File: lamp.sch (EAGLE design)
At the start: 57 parts

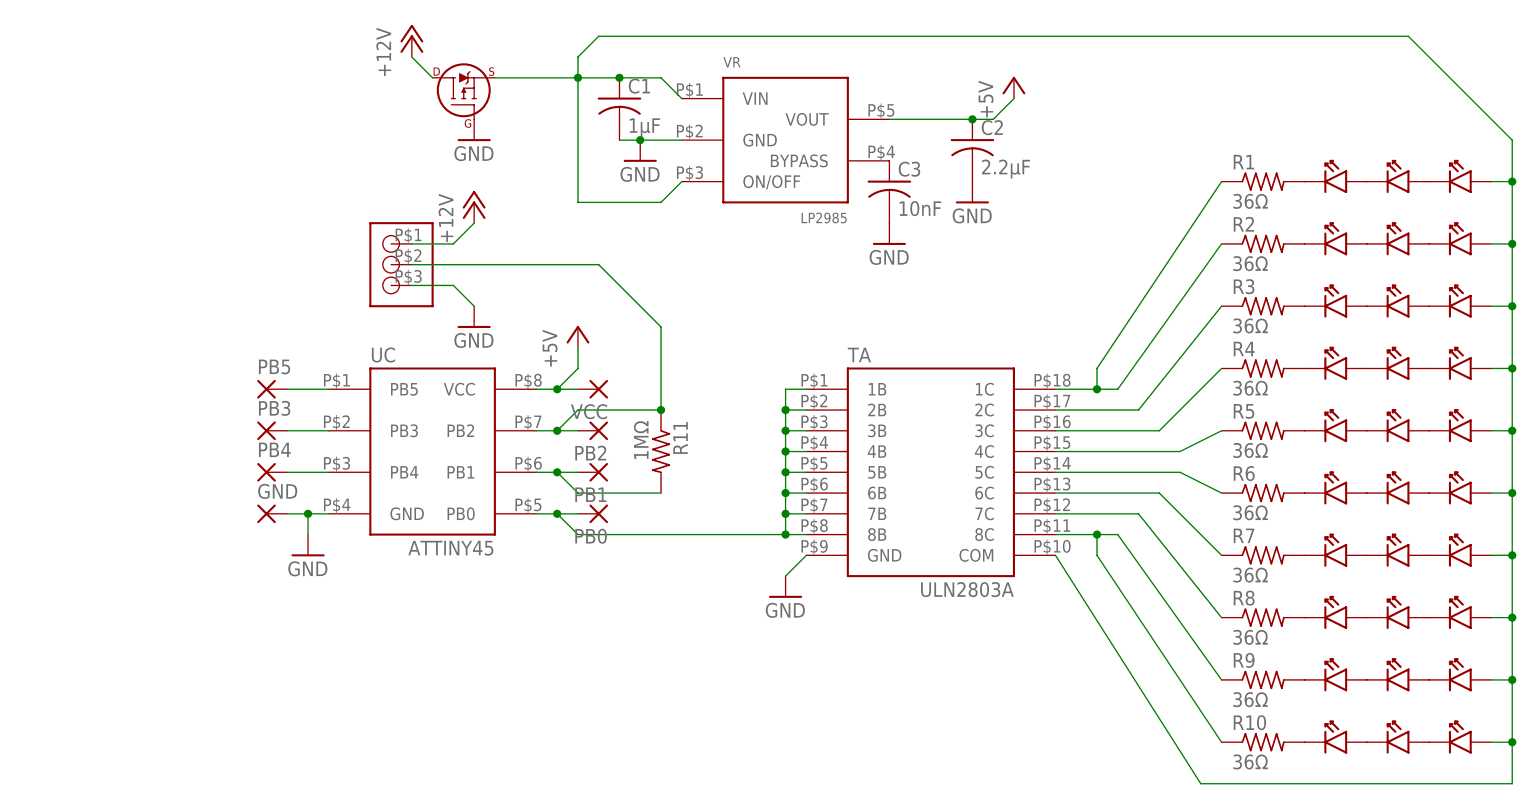
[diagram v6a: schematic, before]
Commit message: Swapped pins around on attiny45 for a better layout, adjusted layout accordingly. Much cleaner now.
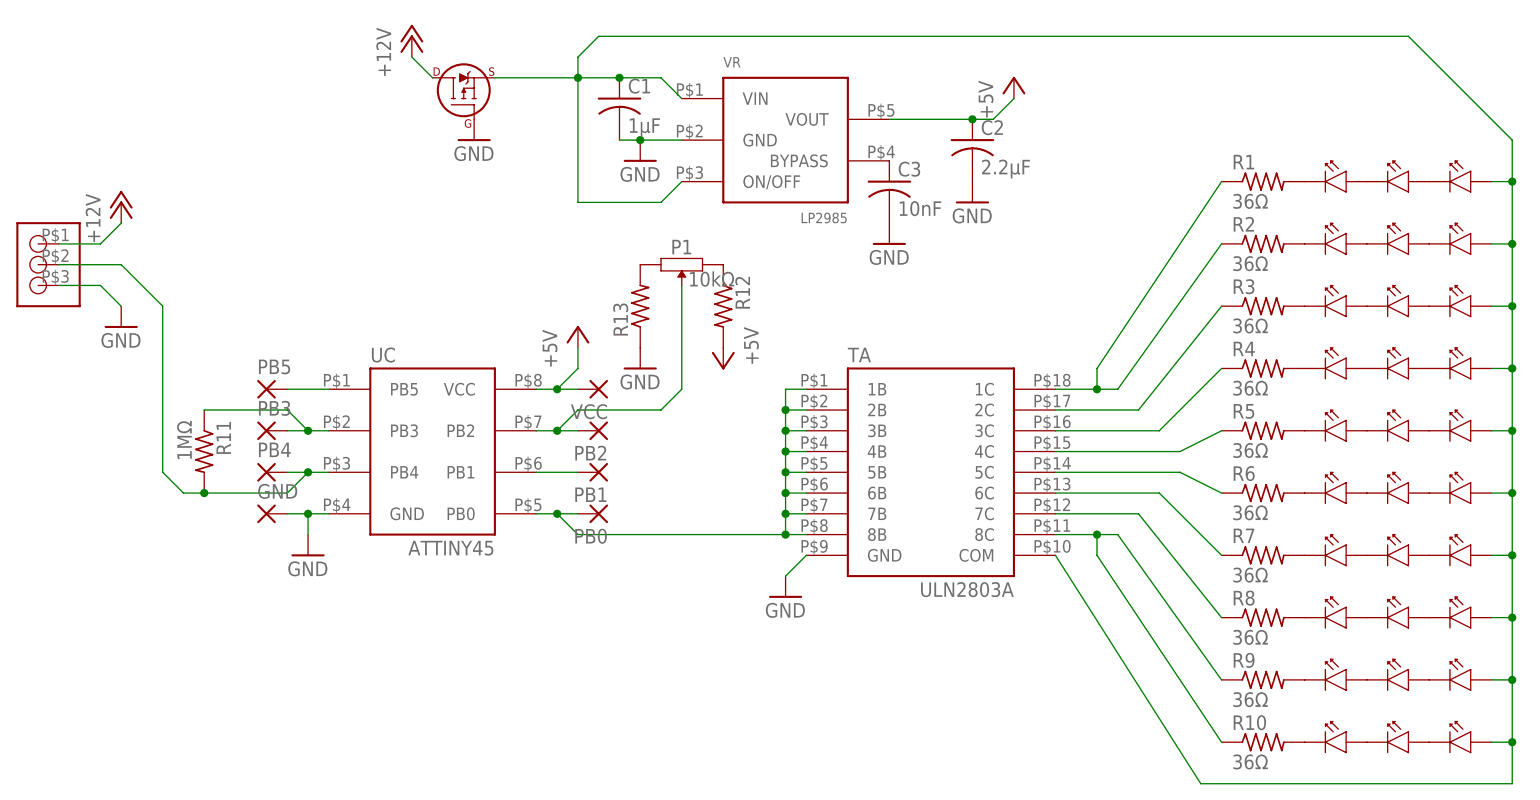
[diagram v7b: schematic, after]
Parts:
- added P1: 10kΩ, lamp:PVG3G
- added R12, R13: (no value), Barebones-Arduino:RESISTOR-SMD
- renumbered U$19 to F1
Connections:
- net +12V renamed N$49
- removed net N$14: PB1.P, R11.2, UC.PB1
- removed net N$39: PB3.P, UC.PB3
- new net N$50: P1.P$2, PB2.P, UC.PB2
- new net N$51: PB3.P, R11.1, UC.PB3
- new net N$52: PB1.P, UC.PB1
- net +5V: now also C2.1, R12.2, VR.VOUT
- net GND: now also R13.1
- net N$15: now also PB4.P, R11.2, U$32.P$2, UC.PB4; no longer C2.1, VR.VOUT
- net N$17: now also P1.P$3, R12.1; no longer PB2.P, R11.1, U$32.P$2, UC.PB2
- net N$44: now also P1.P$1, R13.2; no longer PB4.P, UC.PB4
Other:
- moved on the sheet: R11
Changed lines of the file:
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@@
 <part name="GND4" library=" Barebones-Arduino" deviceset="GND" device=""/>
 <part name="R11" library=" Barebones-Arduino" deviceset="RESISTOR" device="-SMD" value="1MΩ"/>
-<part name="U$19" library="lamp" deviceset="SI2319DS" device=""/>
+<part name="F1" library="lamp" deviceset="SI2319DS" device=""/>
 <part name="GND6" library=" Barebones-Arduino" deviceset="GND" device=""/>
 <part name="U$32" library="lamp" deviceset="HEADER-3X1" device=""/>
 <part name="P+5" library=" Barebones-Arduino" deviceset="+12V" device=""/>
 <part name="GND7" library=" Barebones-Arduino" deviceset="GND" device=""/>
+<part name="P1" library="lamp" deviceset="PVG3G" device="" value="10kΩ"/>
+<part name="R12" library=" Barebones-Arduino" deviceset="RESISTOR" device="-SMD"/>
+<part name="R13" library=" Barebones-Arduino" deviceset="RESISTOR" device="-SMD"/>
+<part name="P+1" library=" Barebones-Arduino" deviceset="+5V" device=""/>
+<part name="GND8" library=" Barebones-Arduino" deviceset="GND" device=""/>
 </parts>
 <sheets>
@@
 <instance part="C3" gate="G$1" x="58.42" y="76.2"/>
 <instance part="GND4" gate="1" x="58.42" y="68.58"/>
-<instance part="R11" gate="G$1" x="30.48" y="43.18" rot="R270"/>
-<instance part="U$19" gate="G$1" x="5.08" y="88.9"/>
+<instance part="R11" gate="G$1" x="-25.4" y="43.18" rot="R270"/>
+<instance part="F1" gate="G$1" x="5.08" y="88.9"/>
 <instance part="GND6" gate="1" x="7.62" y="81.28"/>
-<instance part="U$32" gate="G$1" x="0" y="68.58"/>
-<instance part="P+5" gate="1" x="7.62" y="73.66"/>
-<instance part="GND7" gate="1" x="7.62" y="58.42"/>
+<instance part="U$32" gate="G$1" x="-43.18" y="68.58"/>
+<instance part="P+5" gate="1" x="-35.56" y="73.66"/>
+<instance part="GND7" gate="1" x="-35.56" y="58.42"/>
+<instance part="P1" gate="G$1" x="33.02" y="66.04" rot="R90"/>
+<instance part="R12" gate="G$1" x="38.1" y="60.96" rot="R270"/>
+<instance part="R13" gate="G$1" x="27.94" y="60.96" rot="R90"/>
+<instance part="P+1" gate="1" x="38.1" y="53.34" rot="R180"/>
+<instance part="GND8" gate="1" x="27.94" y="53.34"/>
 </instances>
 <busses>
@@
 </segment>
 </net>
-<net name="+12V" class="0">
+<net name="N$49" class="0">
 <segment>
 <pinref part="P+3" gate="1" pin="+12V"/>
-<pinref part="U$19" gate="G$1" pin="DRAIN"/>
+<pinref part="F1" gate="G$1" pin="DRAIN"/>
 <wire x1="0" y1="91.44" x2="2.54" y2="88.9" width="0.1524" layer="91"/>
 </segment>
 <segment>
 <pinref part="U$32" gate="G$1" pin="P$1"/>
-<wire x1="0" y1="68.58" x2="5.08" y2="68.58" width="0.1524" layer="91"/>
-<wire x1="5.08" y1="68.58" x2="7.62" y2="71.12" width="0.1524" layer="91"/>
+<wire x1="-43.18" y1="68.58" x2="-38.1" y2="68.58" width="0.1524" layer="91"/>
+<wire x1="-38.1" y1="68.58" x2="-35.56" y2="71.12" width="0.1524" layer="91"/>
 <pinref part="P+5" gate="1" pin="+12V"/>
 </segment>
@@
 </segment>
 <segment>
-<pinref part="U$19" gate="G$1" pin="GATE"/>
+<pinref part="F1" gate="G$1" pin="GATE"/>
 <pinref part="GND6" gate="1" pin="GND"/>
 </segment>
 <segment>
 <pinref part="U$32" gate="G$1" pin="P$3"/>
-<wire x1="0" y1="63.5" x2="5.08" y2="63.5" width="0.1524" layer="91"/>
-<wire x1="7.62" y1="60.96" x2="5.08" y2="63.5" width="0.1524" layer="91"/>
+<wire x1="-43.18" y1="63.5" x2="-38.1" y2="63.5" width="0.1524" layer="91"/>
+<wire x1="-35.56" y1="60.96" x2="-38.1" y2="63.5" width="0.1524" layer="91"/>
 <pinref part="GND7" gate="1" pin="GND"/>
 </segment>
-</net>
-<net name="N$15" class="0">
-<segment>
-<pinref part="P+4" gate="1" pin="+5V"/>
-<wire x1="73.66" y1="86.36" x2="71.12" y2="83.82" width="0.1524" layer="91"/>
-<pinref part="VR" gate="G$1" pin="VOUT"/>
-<pinref part="C2" gate="G$1" pin="1"/>
-<wire x1="58.42" y1="83.82" x2="68.58" y2="83.82" width="0.1524" layer="91"/>
-<junction x="68.58" y="83.82"/>
-<wire x1="71.12" y1="83.82" x2="68.58" y2="83.82" width="0.1524" layer="91"/>
-</segment>
-</net>
-<net name="N$14" class="0">
-<segment>
-<pinref part="UC" gate="G$1" pin="PB1"/>
-<pinref part="PB1" gate="1" pin="P"/>
-<wire x1="15.24" y1="40.64" x2="17.78" y2="40.64" width="0.1524" layer="91"/>
-<pinref part="R11" gate="G$1" pin="2"/>
-<wire x1="17.78" y1="40.64" x2="20.32" y2="40.64" width="0.1524" layer="91"/>
-<wire x1="17.78" y1="40.64" x2="20.32" y2="38.1" width="0.1524" layer="91"/>
-<wire x1="20.32" y1="38.1" x2="30.48" y2="38.1" width="0.1524" layer="91"/>
-<junction x="17.78" y="40.64"/>
-</segment>
-</net>
-<net name="N$17" class="0">
-<segment>
-<pinref part="UC" gate="G$1" pin="PB2"/>
-<pinref part="PB2" gate="1" pin="P"/>
-<wire x1="15.24" y1="45.72" x2="17.78" y2="45.72" width="0.1524" layer="91"/>
-<pinref part="R11" gate="G$1" pin="1"/>
-<wire x1="17.78" y1="45.72" x2="20.32" y2="45.72" width="0.1524" layer="91"/>
-<wire x1="17.78" y1="45.72" x2="20.32" y2="48.26" width="0.1524" layer="91"/>
-<wire x1="20.32" y1="48.26" x2="30.48" y2="48.26" width="0.1524" layer="91"/>
-<junction x="17.78" y="45.72"/>
-<junction x="30.48" y="48.26"/>
-<pinref part="U$32" gate="G$1" pin="P$2"/>
-<wire x1="0" y1="66.04" x2="22.86" y2="66.04" width="0.1524" layer="91"/>
-<wire x1="22.86" y1="66.04" x2="30.48" y2="58.42" width="0.1524" layer="91"/>
-<wire x1="30.48" y1="58.42" x2="30.48" y2="48.26" width="0.1524" layer="91"/>
+<segment>
+<pinref part="R13" gate="G$1" pin="1"/>
+<pinref part="GND8" gate="1" pin="GND"/>
 </segment>
 </net>
@@
 <pinref part="PB5" gate="1" pin="P"/>
 <wire x1="-10.16" y1="50.8" x2="-15.24" y2="50.8" width="0.1524" layer="91"/>
-</segment>
-</net>
-<net name="N$39" class="0">
-<segment>
-<pinref part="UC" gate="G$1" pin="PB3"/>
-<pinref part="PB3" gate="1" pin="P"/>
-<wire x1="-10.16" y1="45.72" x2="-15.24" y2="45.72" width="0.1524" layer="91"/>
-</segment>
-</net>
-<net name="N$44" class="0">
-<segment>
-<pinref part="UC" gate="G$1" pin="PB4"/>
-<pinref part="PB4" gate="1" pin="P"/>
-<wire x1="-10.16" y1="40.64" x2="-15.24" y2="40.64" width="0.1524" layer="91"/>
 </segment>
 </net>
@@
 <junction x="17.78" y="50.8"/>
 </segment>
+<segment>
+<pinref part="P+4" gate="1" pin="+5V"/>
+<wire x1="73.66" y1="86.36" x2="71.12" y2="83.82" width="0.1524" layer="91"/>
+<pinref part="VR" gate="G$1" pin="VOUT"/>
+<pinref part="C2" gate="G$1" pin="1"/>
+<wire x1="58.42" y1="83.82" x2="68.58" y2="83.82" width="0.1524" layer="91"/>
+<junction x="68.58" y="83.82"/>
+<wire x1="71.12" y1="83.82" x2="68.58" y2="83.82" width="0.1524" layer="91"/>
+</segment>
+<segment>
+<pinref part="R12" gate="G$1" pin="2"/>
+<pinref part="P+1" gate="1" pin="+5V"/>
+</segment>
 </net>
 <net name="N$45" class="0">
@@
 <pinref part="VR" gate="G$1" pin="VIN"/>
 <wire x1="30.48" y1="88.9" x2="33.02" y2="86.36" width="0.1524" layer="91"/>
-<pinref part="U$19" gate="G$1" pin="SOURCE"/>
+<pinref part="F1" gate="G$1" pin="SOURCE"/>
 <wire x1="10.16" y1="88.9" x2="20.32" y2="88.9" width="0.1524" layer="91"/>
 <junction x="20.32" y="88.9"/>
@@
 </segment>
 </net>
+<net name="N$15" class="0">
+<segment>
+<pinref part="PB4" gate="1" pin="P"/>
+<pinref part="UC" gate="G$1" pin="PB4"/>
+<wire x1="-10.16" y1="40.64" x2="-12.7" y2="40.64" width="0.1524" layer="91"/>
+<pinref part="R11" gate="G$1" pin="2"/>
+<wire x1="-12.7" y1="40.64" x2="-15.24" y2="40.64" width="0.1524" layer="91"/>
+<wire x1="-12.7" y1="40.64" x2="-15.24" y2="38.1" width="0.1524" layer="91"/>
+<wire x1="-15.24" y1="38.1" x2="-25.4" y2="38.1" width="0.1524" layer="91"/>
+<junction x="-12.7" y="40.64"/>
+<wire x1="-25.4" y1="38.1" x2="-27.94" y2="38.1" width="0.1524" layer="91"/>
+<junction x="-25.4" y="38.1"/>
+<wire x1="-27.94" y1="38.1" x2="-30.48" y2="40.64" width="0.1524" layer="91"/>
+<wire x1="-30.48" y1="40.64" x2="-30.48" y2="60.96" width="0.1524" layer="91"/>
+<pinref part="U$32" gate="G$1" pin="P$2"/>
+<wire x1="-30.48" y1="60.96" x2="-35.56" y2="66.04" width="0.1524" layer="91"/>
+<wire x1="-35.56" y1="66.04" x2="-43.18" y2="66.04" width="0.1524" layer="91"/>
+</segment>
+</net>
+<net name="N$17" class="0">
+<segment>
+<pinref part="P1" gate="G$1" pin="P$3"/>
+<pinref part="R12" gate="G$1" pin="1"/>
+</segment>
+</net>
+<net name="N$44" class="0">
+<segment>
+<pinref part="P1" gate="G$1" pin="P$1"/>
+<pinref part="R13" gate="G$1" pin="2"/>
+</segment>
+</net>
+<net name="N$50" class="0">
+<segment>
+<pinref part="PB2" gate="1" pin="P"/>
+<pinref part="UC" gate="G$1" pin="PB2"/>
+<wire x1="15.24" y1="45.72" x2="17.78" y2="45.72" width="0.1524" layer="91"/>
+<wire x1="17.78" y1="45.72" x2="20.32" y2="45.72" width="0.1524" layer="91"/>
+<wire x1="17.78" y1="45.72" x2="20.32" y2="48.26" width="0.1524" layer="91"/>
+<wire x1="20.32" y1="48.26" x2="30.48" y2="48.26" width="0.1524" layer="91"/>
+<junction x="17.78" y="45.72"/>
+<pinref part="P1" gate="G$1" pin="P$2"/>
+<wire x1="30.48" y1="48.26" x2="33.02" y2="50.8" width="0.1524" layer="91"/>
+<wire x1="33.02" y1="50.8" x2="33.02" y2="63.5" width="0.1524" layer="91"/>
+</segment>
+</net>
+<net name="N$52" class="0">
+<segment>
+<pinref part="PB1" gate="1" pin="P"/>
+<pinref part="UC" gate="G$1" pin="PB1"/>
+<wire x1="15.24" y1="40.64" x2="20.32" y2="40.64" width="0.1524" layer="91"/>
+</segment>
+</net>
+<net name="N$51" class="0">
+<segment>
+<pinref part="R11" gate="G$1" pin="1"/>
+<pinref part="PB3" gate="1" pin="P"/>
+<pinref part="UC" gate="G$1" pin="PB3"/>
+<wire x1="-10.16" y1="45.72" x2="-12.7" y2="45.72" width="0.1524" layer="91"/>
+<wire x1="-12.7" y1="45.72" x2="-15.24" y2="45.72" width="0.1524" layer="91"/>
+<junction x="-12.7" y="45.72"/>
+<wire x1="-12.7" y1="45.72" x2="-15.24" y2="48.26" width="0.1524" layer="91"/>
+<wire x1="-15.24" y1="48.26" x2="-25.4" y2="48.26" width="0.1524" layer="91"/>
+</segment>
+</net>

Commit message: A little more schematic fine-tuning and board arrangement. Nothing significant.
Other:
- moved on the sheet: R12, R13
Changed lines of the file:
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@@
 <instance part="GND7" gate="1" x="-35.56" y="58.42"/>
 <instance part="P1" gate="G$1" x="33.02" y="66.04" rot="R90"/>
-<instance part="R12" gate="G$1" x="38.1" y="60.96" rot="R270"/>
-<instance part="R13" gate="G$1" x="27.94" y="60.96" rot="R90"/>
-<instance part="P+1" gate="1" x="38.1" y="53.34" rot="R180"/>
-<instance part="GND8" gate="1" x="27.94" y="53.34"/>
+<instance part="R12" gate="G$1" x="43.18" y="66.04"/>
+<instance part="R13" gate="G$1" x="22.86" y="66.04"/>
+<instance part="P+1" gate="1" x="50.8" y="60.96" rot="R180"/>
+<instance part="GND8" gate="1" x="15.24" y="60.96"/>
 </instances>
 <busses>
@@
 <pinref part="R13" gate="G$1" pin="1"/>
 <pinref part="GND8" gate="1" pin="GND"/>
+<wire x1="17.78" y1="66.04" x2="15.24" y2="63.5" width="0.1524" layer="91"/>
 </segment>
 </net>
@@
 <pinref part="R12" gate="G$1" pin="2"/>
 <pinref part="P+1" gate="1" pin="+5V"/>
-</segment>
-</net>
+<wire x1="48.26" y1="66.04" x2="50.8" y2="63.5" width="0.1524" layer="91"/>
+</segment>
+</net>
